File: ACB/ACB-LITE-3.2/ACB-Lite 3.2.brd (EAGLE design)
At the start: 63.5 x 226.8 mm, 246 parts, among them CON2 166087-4, IC1 PIC32MX470F512L-I/PF, IC10 MAX9938HEUK+T, IC11 24LC32A-I/MS, IC12 SN65HVD12D, IC13 REF3025, IC14 TPD2E001DZDR, IC15 TPD2E001DZDR, IC16 MCP6042-I/MS, IC2 L6227Q, IC3 LT3971EMSE, IC6 MIC841LYC, IC7 24LC32A-I/MS, IC9 AT25SF321-SSHD, J1 3-641215-2, J12 USB_A_180, J13 3-641215-2, J14 3-641215-5, J15 3-641215-5, J17 DNP-open-hole, J2 3-641215-2, J3 RJ8-8-180, J4 RJ8-8-180, J5 3-641215-2, J6 3-641215-2, J7 3-641215-2, Q1 SSM6P49NU,LFPZ, Q2 SSM6P49NU,LFPZ, Q3 FDC6330L, Q4 FDG6303N, Q5 FDC6506P, Q6 FDG6303N, Q7 FDC6506P, T1 PIC-OUT, T13 PIC-RPX, T14 PIC-RPX, T15 PIC-OUT, T27 PIC-OUT, T3 PIC-RPX, T32 PIC-OUT, T33 PIC-OUT, T36 PIC-OUT, T37 PIN-AN, T38 PIN-AN, T39 PIN-AN, T40 PIC-RPX, T41 PIC-RPX, T42 PIC-OUT, T43 PIC-RPX, T44 PIC-OUT, T45 PIC-RPX, T5 PIC-OUT, T7 PIC-OUT, X1 8MHz-5x3.2mm

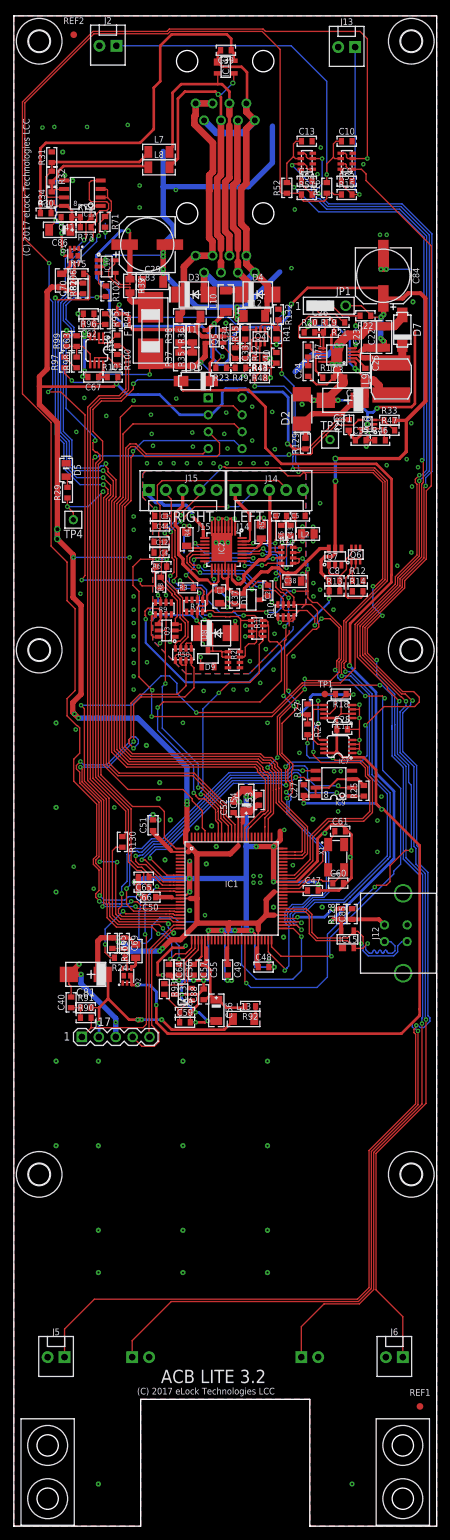
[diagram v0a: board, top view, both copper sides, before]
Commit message: adeded ACB LITE 3.2 with fab files
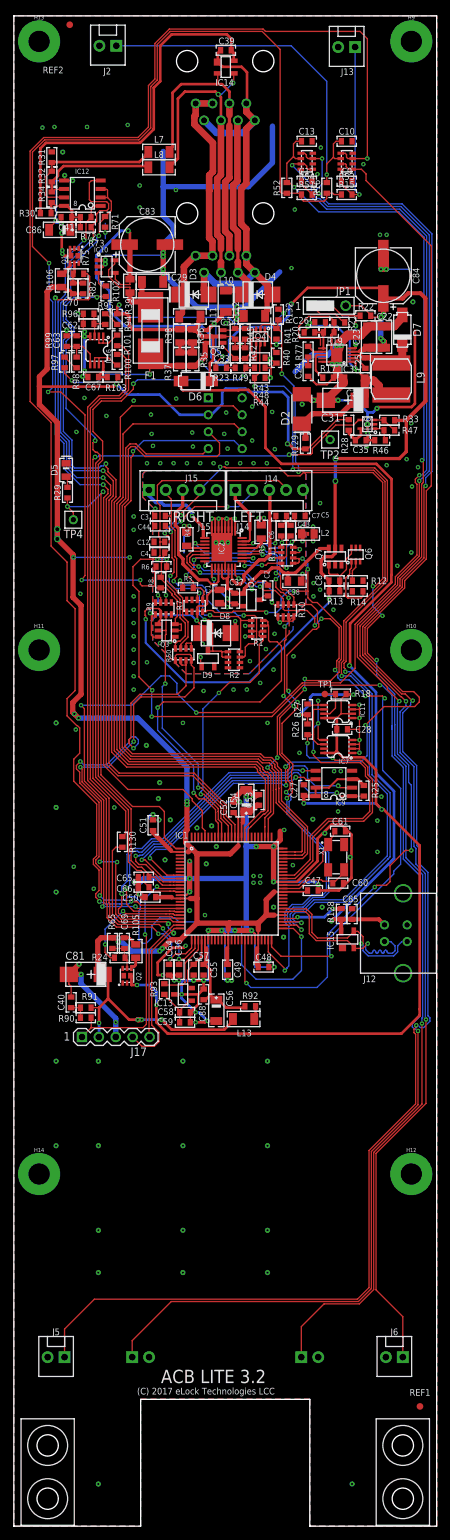
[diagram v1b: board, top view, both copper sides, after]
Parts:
- removed H3, H4, H5, H6, H7, H8: MOUNT-HOLE3.2, holes:3,2
- added H10, H11, H12, H13, H14, H9: STANDOFF_ELECTRICAL, SparkFun-Hardware:STANDOFF-ELECTRICAL
- moved REF2 1.62 mm to (8.40, 225.5)
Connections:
- net DGND: now also H10.P1, H11.P1, H12.P1, H13.P1, H14.P1, H9.P1
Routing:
- net N$40: track 179.7 -> 180.5 mm
- net PAL2: track 219.8 -> 220.7 mm
